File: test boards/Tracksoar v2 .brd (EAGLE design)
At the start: 50.4 x 19.6 mm, 48 parts, among them IC1 BME280, IC2 74AHC1G125DBV, Y1 16MHZ

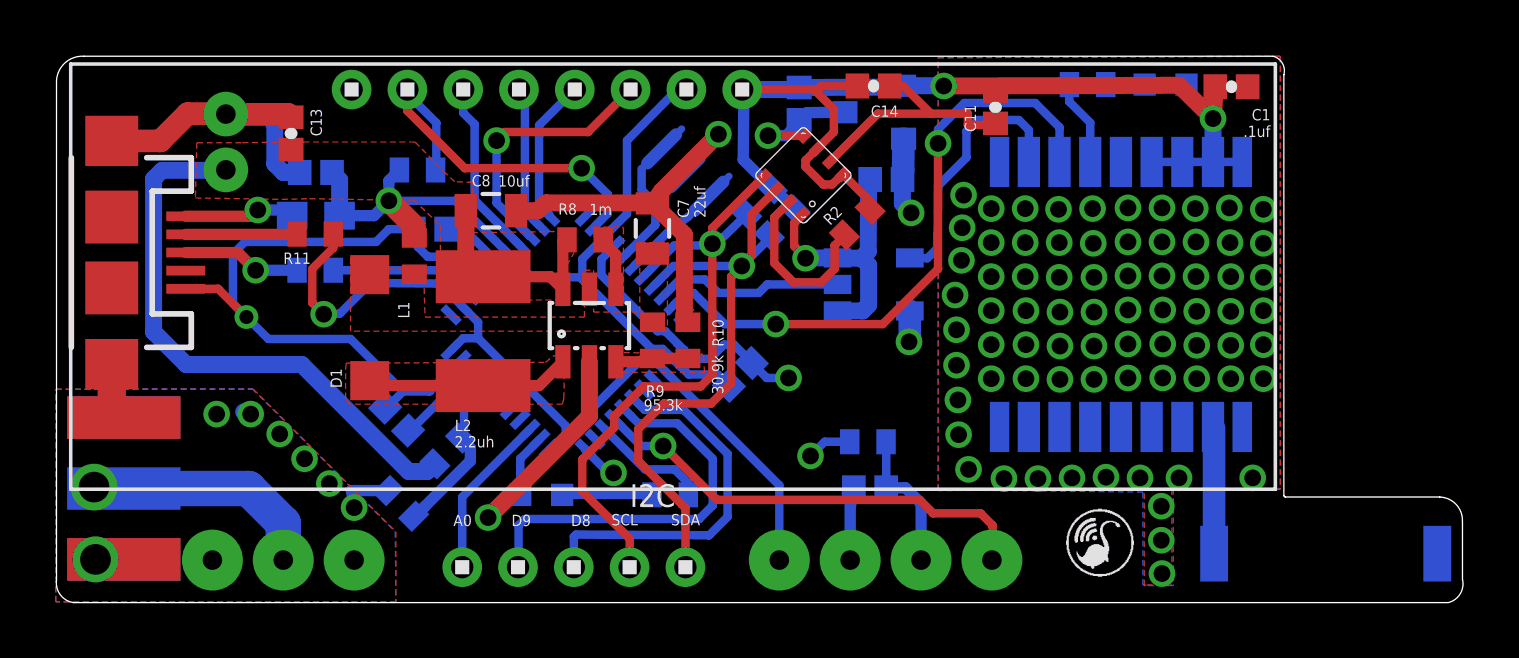
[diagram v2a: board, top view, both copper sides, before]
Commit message: Swapped Serial1 RX and TX
Fixed an issue sending / receiving serial between the atmega32u4 and
ublox max m8q by swapping the rx and tx pins on the atmega32u4.
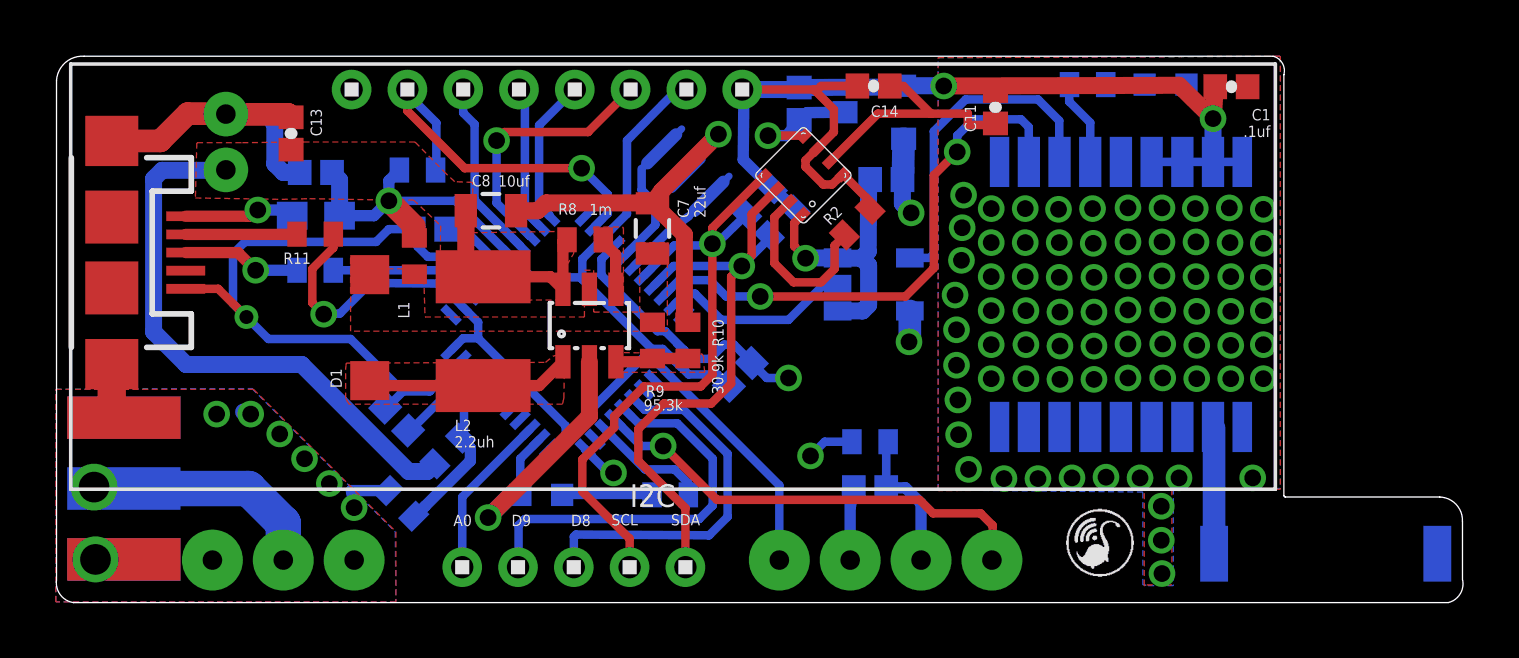
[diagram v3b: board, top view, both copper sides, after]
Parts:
- moved R12 0.08 mm to (29.2, 5.74)
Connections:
- net RX: now also U$1.2_TXD1, U$4.20; no longer U$1.3_RXD1, U$4.21
- net TX: now also U$4.21; no longer U$4.20
- net TX1: now also U$1.3_RXD1; no longer U$1.2_TXD1
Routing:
- net TX1: track 9.45 -> 12.1 mm
- net RX: track 22.3 -> 19.8 mm
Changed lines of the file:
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@@
 <layers>
 <layer number="1" name="Top" color="4" fill="1" visible="yes" active="yes"/>
-<layer number="2" name="Route2" color="6" fill="1" visible="yes" active="yes"/>
+<layer number="2" name="Route2" color="6" fill="1" visible="no" active="yes"/>
 <layer number="3" name="Route3" color="4" fill="3" visible="no" active="no"/>
 <layer number="14" name="Route14" color="1" fill="6" visible="no" active="no"/>
-<layer number="15" name="Route15" color="3" fill="1" visible="yes" active="yes"/>
+<layer number="15" name="Route15" color="3" fill="1" visible="no" active="yes"/>
 <layer number="16" name="Bottom" color="1" fill="1" visible="yes" active="yes"/>
 <layer number="17" name="Pads" color="2" fill="1" visible="yes" active="yes"/>
@@
 <element name="C12" library="SparkFun-Capacitors" package="0402-CAP" value="1uf" x="12.2174" y="6.5532" rot="MR225"/>
 <element name="C13" library="SparkFun-Capacitors" package="0402-CAP" value=".1uf" x="8.4328" y="16.7894" rot="R270"/>
-<element name="C14" library="SparkFun-Capacitors" package="0402-CAP" value=".1uf" x="29.3116" y="18.4912" rot="R180"/>
-<element name="R12" library="adafruit" package="R0402" value="10k" x="29.1084" y="5.7404" smashed="yes" rot="MR0">
-<attribute name="NAME" x="30.226" y="6.477" size="0.4064" layer="26" rot="MR0"/>
-<attribute name="VALUE" x="28.9052" y="6.4516" size="0.4064" layer="28" rot="MR0"/>
+<element name="C14" library="SparkFun-Capacitors" package="0402-CAP" value=".1uf" x="29.3116" y="18.4912" smashed="yes" rot="R180">
+<attribute name="NAME" x="30.2006" y="17.7927" size="0.4064" layer="25" rot="R180"/>
+<attribute name="VALUE" x="28.9687" y="17.78" size="0.4064" layer="27" rot="R180"/>
+</element>
+<element name="R12" library="adafruit" package="R0402" value="10k" x="29.1846" y="5.7404" smashed="yes" rot="MR0">
+<attribute name="NAME" x="30.3022" y="6.477" size="0.4064" layer="26" rot="MR0"/>
+<attribute name="VALUE" x="28.9814" y="6.4516" size="0.4064" layer="28" rot="MR0"/>
 </element>
 </elements>
@@
 <wire x1="30.3784" y1="18.4912" x2="31.369" y2="17.5006" width="0.3048" layer="1"/>
 <contactref element="R12" pad="1"/>
-<wire x1="29.7584" y1="5.7404" x2="29.7646" y2="5.7342" width="0.3048" layer="16"/>
+<wire x1="29.8346" y1="5.7404" x2="29.7646" y2="5.7342" width="0.3048" layer="16"/>
 <wire x1="29.7646" y1="5.7342" x2="29.7646" y2="4.0894" width="0.3048" layer="16"/>
 <wire x1="24.946525" y1="8.563521875" x2="25.483646875" y2="8.0264" width="0.3048" layer="16"/>
@@
 <signal name="TX1">
 <contactref element="IC2" pad="4"/>
-<contactref element="U$1" pad="2_TXD1"/>
-<wire x1="34.877" y1="15.7704" x2="34.877" y2="16.9136" width="0.3048" layer="16"/>
-<wire x1="34.877" y1="16.9136" x2="34.5186" y2="17.272" width="0.3048" layer="16"/>
-<wire x1="34.5186" y1="17.272" x2="33.0454" y2="17.272" width="0.3048" layer="16"/>
-<wire x1="33.0454" y1="17.272" x2="32.639" y2="16.8656" width="0.3048" layer="16"/>
-<wire x1="32.639" y1="16.8656" x2="32.639" y2="15.9258" width="0.3048" layer="16"/>
-<wire x1="32.639" y1="15.9258" x2="31.623" y2="14.9098" width="0.3048" layer="16"/>
-<wire x1="31.623" y1="14.9098" x2="31.5976" y2="12.6746" width="0.3048" layer="16"/>
-<wire x1="31.5976" y1="12.6746" x2="31.242" y2="12.319" width="0.3048" layer="16"/>
-<wire x1="31.242" y1="12.319" x2="30.6218" y2="12.319" width="0.3048" layer="16"/>
-<wire x1="30.6218" y1="12.319" x2="30.6116" y2="12.3292" width="0.3048" layer="16"/>
+<contactref element="U$1" pad="3_RXD1"/>
+<wire x1="30.6116" y1="12.3292" x2="31.3284" y2="12.3292" width="0.3048" layer="16"/>
+<wire x1="31.3284" y1="12.3292" x2="31.4706" y2="12.446" width="0.3048" layer="16"/>
+<wire x1="31.4706" y1="12.446" x2="31.4706" y2="16.8656" width="0.3048" layer="16"/>
+<wire x1="31.4706" y1="16.8656" x2="32.6136" y2="18.0086" width="0.3048" layer="16"/>
+<wire x1="32.6136" y1="18.0086" x2="35.2044" y2="18.0086" width="0.3048" layer="16"/>
+<wire x1="35.2044" y1="18.0086" x2="35.9664" y2="17.2466" width="0.3048" layer="16"/>
+<wire x1="35.9664" y1="17.2466" x2="35.9664" y2="15.781" width="0.3048" layer="16"/>
+<wire x1="35.9664" y1="15.781" x2="35.977" y2="15.7704" width="0.3048" layer="16"/>
 </signal>
 <signal name="VDDD">
@@
 </signal>
 <signal name="TX">
+<contactref element="IC2" pad="2"/>
+<contactref element="U$4" pad="21"/>
+<wire x1="22.157178125" y1="10.641946875" x2="22.56423125" y2="11.049" width="0.3048" layer="16"/>
+<wire x1="22.56423125" y1="11.049" x2="22.9108" y2="11.049" width="0.3048" layer="16"/>
+<wire x1="22.9108" y1="11.049" x2="23.8506" y2="10.1092" width="0.3048" layer="16"/>
+<wire x1="23.8506" y1="10.1092" x2="26.2636" y2="10.1092" width="0.3048" layer="16"/>
+<wire x1="26.2636" y1="10.1092" x2="27.5082" y2="11.3538" width="0.3048" layer="16"/>
+<wire x1="27.5082" y1="11.3538" x2="27.9962" y2="11.3538" width="0.3048" layer="16"/>
+<wire x1="27.9962" y1="11.3538" x2="28.0216" y2="11.3792" width="0.3048" layer="16"/>
+</signal>
+<signal name="RX">
 <contactref element="U$4" pad="20"/>
-<contactref element="IC2" pad="2"/>
-<wire x1="21.803625" y1="10.9955" x2="22.365125" y2="11.557" width="0.3048" layer="16"/>
-<wire x1="22.365125" y1="11.557" x2="23.2664" y2="11.557" width="0.3048" layer="16"/>
-<wire x1="23.2664" y1="11.557" x2="23.749" y2="11.0744" width="0.3048" layer="16"/>
-<wire x1="23.749" y1="11.0744" x2="25.1968" y2="11.0744" width="0.3048" layer="16"/>
-<wire x1="25.1968" y1="11.0744" x2="25.5016" y2="11.3792" width="0.3048" layer="16"/>
-<wire x1="25.5016" y1="11.3792" x2="28.0216" y2="11.3792" width="0.3048" layer="16"/>
-</signal>
-<signal name="RX">
-<contactref element="U$4" pad="21"/>
-<contactref element="U$1" pad="3_RXD1"/>
-<wire x1="22.157178125" y1="10.641946875" x2="22.58963125" y2="11.0744" width="0.3048" layer="16"/>
-<wire x1="29.6418" y1="9.9568" x2="31.623" y2="11.938" width="0.3048" layer="1"/>
-<wire x1="31.623" y1="11.938" x2="31.623" y2="16.4338" width="0.3048" layer="1"/>
-<via x="31.623" y="16.4338" extent="1-16" drill="0.6"/>
-<wire x1="22.58963125" y1="11.0744" x2="22.86" y2="11.0744" width="0.3048" layer="16"/>
-<wire x1="22.86" y1="11.0744" x2="23.9776" y2="9.9568" width="0.3048" layer="16"/>
-<wire x1="35.977" y1="15.7704" x2="35.977" y2="17.0074" width="0.3048" layer="16"/>
-<wire x1="35.977" y1="17.0074" x2="35.1028" y2="17.8816" width="0.3048" layer="16"/>
-<wire x1="35.1028" y1="17.8816" x2="32.5628" y2="17.8816" width="0.3048" layer="16"/>
-<wire x1="32.5628" y1="17.8816" x2="31.623" y2="16.9418" width="0.3048" layer="16"/>
-<wire x1="31.623" y1="16.9418" x2="31.623" y2="16.4338" width="0.3048" layer="16"/>
-<wire x1="23.9776" y1="9.9568" x2="25.8064" y2="9.9568" width="0.3048" layer="16"/>
-<via x="25.8064" y="9.9568" extent="1-16" drill="0.6"/>
-<wire x1="25.8064" y1="9.9568" x2="29.6418" y2="9.9568" width="0.3048" layer="1"/>
+<contactref element="U$1" pad="2_TXD1"/>
+<wire x1="21.803625" y1="10.9955" x2="22.339725" y2="11.5316" width="0.3048" layer="16"/>
+<wire x1="22.339725" y1="11.5316" x2="23.4442" y2="11.5316" width="0.3048" layer="16"/>
+<wire x1="23.4442" y1="11.5316" x2="24.0284" y2="10.9474" width="0.3048" layer="16"/>
+<wire x1="24.0284" y1="10.9474" x2="25.2476" y2="10.9474" width="0.3048" layer="16"/>
+<via x="25.2476" y="10.9474" extent="1-16" drill="0.6"/>
+<wire x1="25.2476" y1="10.9474" x2="30.4546" y2="10.9474" width="0.3048" layer="1"/>
+<wire x1="30.4546" y1="10.9474" x2="31.4706" y2="11.9634" width="0.3048" layer="1"/>
+<wire x1="31.4706" y1="11.9634" x2="31.4706" y2="15.2908" width="0.3048" layer="1"/>
+<wire x1="31.4706" y1="15.2908" x2="32.3088" y2="16.129" width="0.3048" layer="1"/>
+<via x="32.3088" y="16.129" extent="1-16" drill="0.6"/>
+<wire x1="32.3088" y1="16.129" x2="32.3088" y2="16.7132" width="0.3048" layer="16"/>
+<wire x1="32.3088" y1="16.7132" x2="32.893" y2="17.2974" width="0.3048" layer="16"/>
+<wire x1="32.893" y1="17.2974" x2="34.5948" y2="17.2974" width="0.3048" layer="16"/>
+<wire x1="34.5948" y1="17.2974" x2="34.8742" y2="17.018" width="0.3048" layer="16"/>
+<wire x1="34.8742" y1="17.018" x2="34.8742" y2="15.7732" width="0.3048" layer="16"/>
+<wire x1="34.8742" y1="15.7732" x2="34.877" y2="15.7704" width="0.3048" layer="16"/>
 </signal>
 <signal name="N$20">
@@
 <via x="27.051" y="5.2324" extent="1-16" drill="0.6"/>
 <wire x1="27.051" y1="5.2324" x2="27.559" y2="5.7404" width="0.3048" layer="16"/>
-<wire x1="27.559" y1="5.7404" x2="28.4584" y2="5.7404" width="0.3048" layer="16"/>
+<wire x1="27.559" y1="5.7404" x2="28.5346" y2="5.7404" width="0.3048" layer="16"/>
 </signal>
 </signals>

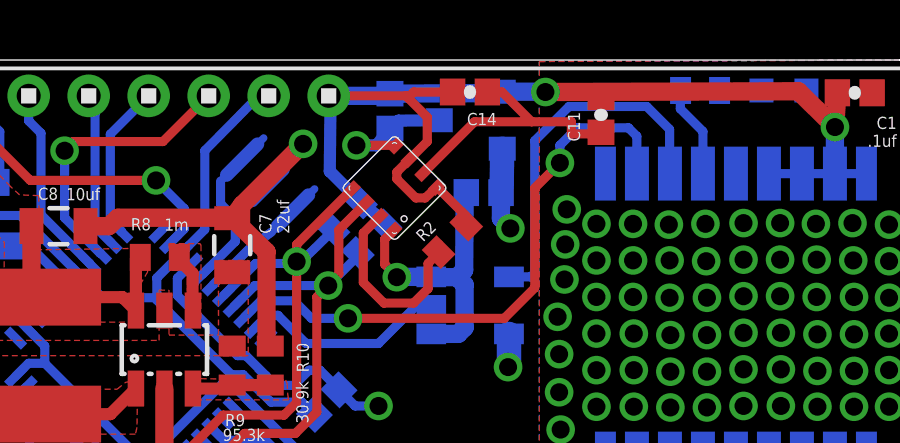
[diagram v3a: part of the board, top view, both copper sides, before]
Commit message: moved bme280 decoupling cap
moved the bme280 decoupling cap a bit for aesthetic reasons.
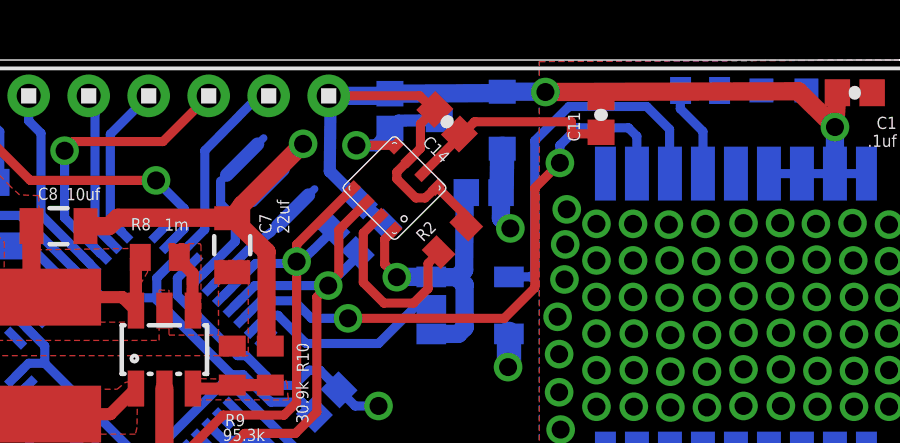
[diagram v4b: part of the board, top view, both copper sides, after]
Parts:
- moved C14 1.25 mm to (28.5, 17.5), turned to 135 degrees
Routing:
- net GND: track 106.2 -> 104.5 mm
- net 3V: track 41.5 -> 40.4 mm
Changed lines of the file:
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@@
 <layers>
 <layer number="1" name="Top" color="4" fill="1" visible="yes" active="yes"/>
-<layer number="2" name="Route2" color="6" fill="1" visible="no" active="yes"/>
+<layer number="2" name="Route2" color="6" fill="1" visible="yes" active="yes"/>
 <layer number="3" name="Route3" color="4" fill="3" visible="no" active="no"/>
 <layer number="14" name="Route14" color="1" fill="6" visible="no" active="no"/>
-<layer number="15" name="Route15" color="3" fill="1" visible="no" active="yes"/>
+<layer number="15" name="Route15" color="3" fill="1" visible="yes" active="yes"/>
 <layer number="16" name="Bottom" color="1" fill="1" visible="yes" active="yes"/>
 <layer number="17" name="Pads" color="2" fill="1" visible="yes" active="yes"/>
@@
 <element name="C12" library="SparkFun-Capacitors" package="0402-CAP" value="1uf" x="12.2174" y="6.5532" rot="MR225"/>
 <element name="C13" library="SparkFun-Capacitors" package="0402-CAP" value=".1uf" x="8.4328" y="16.7894" rot="R270"/>
-<element name="C14" library="SparkFun-Capacitors" package="0402-CAP" value=".1uf" x="29.3116" y="18.4912" smashed="yes" rot="R180">
-<attribute name="NAME" x="30.2006" y="17.7927" size="0.4064" layer="25" rot="R180"/>
-<attribute name="VALUE" x="28.9687" y="17.78" size="0.4064" layer="27" rot="R180"/>
+<element name="C14" library="SparkFun-Capacitors" package="0402-CAP" value=".1uf" x="28.5496" y="17.5006" smashed="yes" rot="R135">
+<attribute name="NAME" x="28.68430625" y="16.378065625" size="0.4064" layer="25" rot="R135"/>
+<attribute name="VALUE" x="27.804240625" y="17.240171875" size="0.4064" layer="27" rot="R135"/>
 </element>
 <element name="R12" library="adafruit" package="R0402" value="10k" x="29.1846" y="5.7404" smashed="yes" rot="MR0">
@@
 <wire x1="17.5768" y1="14.3002" x2="21.2454" y2="14.3002" width="0.6096" layer="1"/>
 <wire x1="21.2454" y1="14.3002" x2="21.3868" y2="14.2858" width="0.6096" layer="1"/>
-<wire x1="27.75159375" y1="15.785771875" x2="29.466421875" y2="17.5006" width="0.3048" layer="1"/>
-<wire x1="29.466421875" y1="17.5006" x2="31.369" y2="17.5006" width="0.3048" layer="1"/>
-<wire x1="31.369" y1="17.5006" x2="32.6898" y2="17.5006" width="0.3048" layer="1"/>
+<wire x1="27.75159375" y1="15.785771875" x2="29.1096125" y2="17.143790625" width="0.3048" layer="1"/>
+<wire x1="29.1096125" y1="17.143790625" x2="29.466421875" y2="17.5006" width="0.3048" layer="1"/>
+<wire x1="29.466421875" y1="17.5006" x2="32.6898" y2="17.5006" width="0.3048" layer="1"/>
 <wire x1="32.6898" y1="17.5006" x2="32.6898" y2="17.0942" width="0.3048" layer="1"/>
 <wire x1="32.6898" y1="17.0942" x2="33.6804" y2="17.0942" width="0.3048" layer="1"/>
@@
 <wire x1="6.6962" y1="17.4846" x2="6.096" y2="17.4846" width="0.8128" layer="1"/>
 <contactref element="C14" pad="1"/>
-<wire x1="29.8916" y1="18.4912" x2="30.3784" y2="18.4912" width="0.3048" layer="1"/>
-<wire x1="30.3784" y1="18.4912" x2="31.369" y2="17.5006" width="0.3048" layer="1"/>
 <contactref element="R12" pad="1"/>
 <wire x1="29.8346" y1="5.7404" x2="29.7646" y2="5.7342" width="0.3048" layer="16"/>
@@
 <wire x1="26.2636" y1="8.0264" x2="26.3652" y2="8.128" width="0.3048" layer="2"/>
 <wire x1="26.3652" y1="8.128" x2="27.1526" y2="8.128" width="0.3048" layer="2"/>
+<wire x1="28.959721875" y1="17.090475" x2="29.0130375" y2="17.143790625" width="0.3048" layer="1"/>
+<wire x1="29.0130375" y1="17.143790625" x2="29.1096125" y2="17.143790625" width="0.3048" layer="1"/>
 </signal>
 <signal name="VCC">
@@
 <wire x1="26.8732" y1="15.8242" x2="27.291971875" y2="16.242971875" width="0.3048" layer="1"/>
 <wire x1="27.291971875" y1="16.242971875" x2="27.291971875" y2="16.24539375" width="0.3048" layer="1"/>
-<wire x1="27.291971875" y1="16.24539375" x2="27.8892" y2="16.842621875" width="0.3048" layer="1"/>
-<wire x1="27.8892" y1="16.842621875" x2="27.8892" y2="17.653" width="0.3048" layer="1"/>
-<wire x1="27.8892" y1="17.653" x2="27.2415" y2="18.3007" width="0.3048" layer="1"/>
-<wire x1="27.2415" y1="18.3007" x2="27.178" y2="18.3642" width="0.3048" layer="1"/>
-<wire x1="27.178" y1="18.3642" x2="24.6022" y2="18.3642" width="0.3048" layer="1"/>
+<wire x1="27.6352" y1="18.3642" x2="24.6022" y2="18.3642" width="0.3048" layer="1"/>
 <wire x1="41.5586" y1="18.4658" x2="41.4886" y2="17.3332" width="0.6096" layer="1"/>
 <wire x1="41.4886" y1="17.3332" x2="41.4782" y2="17.3228" width="0.3048" layer="1"/>
@@
 <wire x1="33.5938" y1="18.4912" x2="33.6804" y2="18.3092" width="0.4064" layer="1"/>
 <contactref element="C14" pad="2"/>
-<wire x1="28.7316" y1="18.4912" x2="27.432" y2="18.4912" width="0.3048" layer="1"/>
-<wire x1="27.432" y1="18.4912" x2="27.2415" y2="18.3007" width="0.3048" layer="1"/>
+<wire x1="27.6352" y1="18.3642" x2="28.088678125" y2="17.910721875" width="0.3048" layer="1"/>
+<wire x1="28.088678125" y1="17.910721875" x2="28.139475" y2="17.910721875" width="0.3048" layer="1"/>
+<wire x1="27.291971875" y1="16.24539375" x2="27.6606" y2="16.614021875" width="0.3048" layer="1"/>
+<wire x1="27.6606" y1="16.614021875" x2="27.6606" y2="17.4244" width="0.3048" layer="1"/>
+<wire x1="27.6606" y1="17.4244" x2="28.139475" y2="17.903275" width="0.3048" layer="1"/>
+<wire x1="28.139475" y1="17.903275" x2="28.139475" y2="17.910721875" width="0.3048" layer="1"/>
 </signal>
 <signal name="N$1">
